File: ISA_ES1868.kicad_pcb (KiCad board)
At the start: 2 copper layers, 104.1 x 102.9 mm, 14 parts, among them J1 ISA BUS

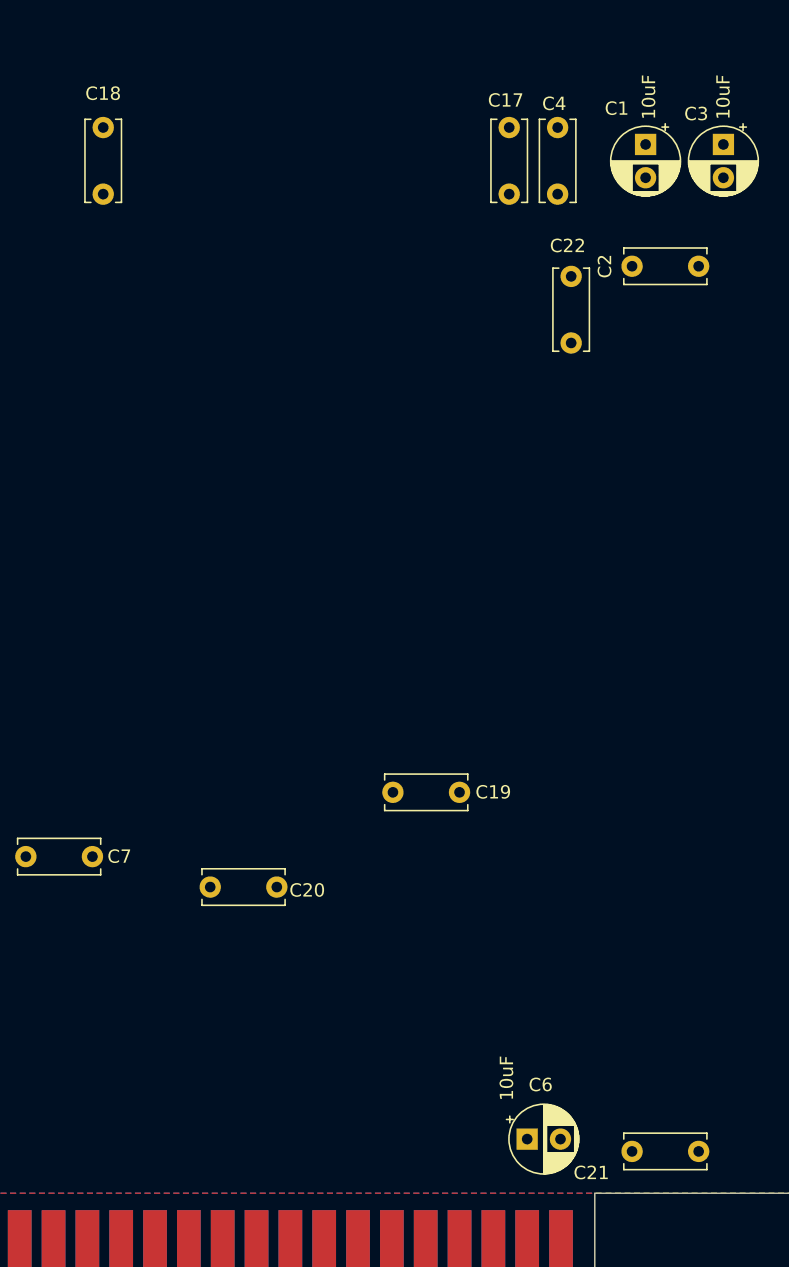
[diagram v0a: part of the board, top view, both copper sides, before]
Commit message: Remove some unused connections from edge
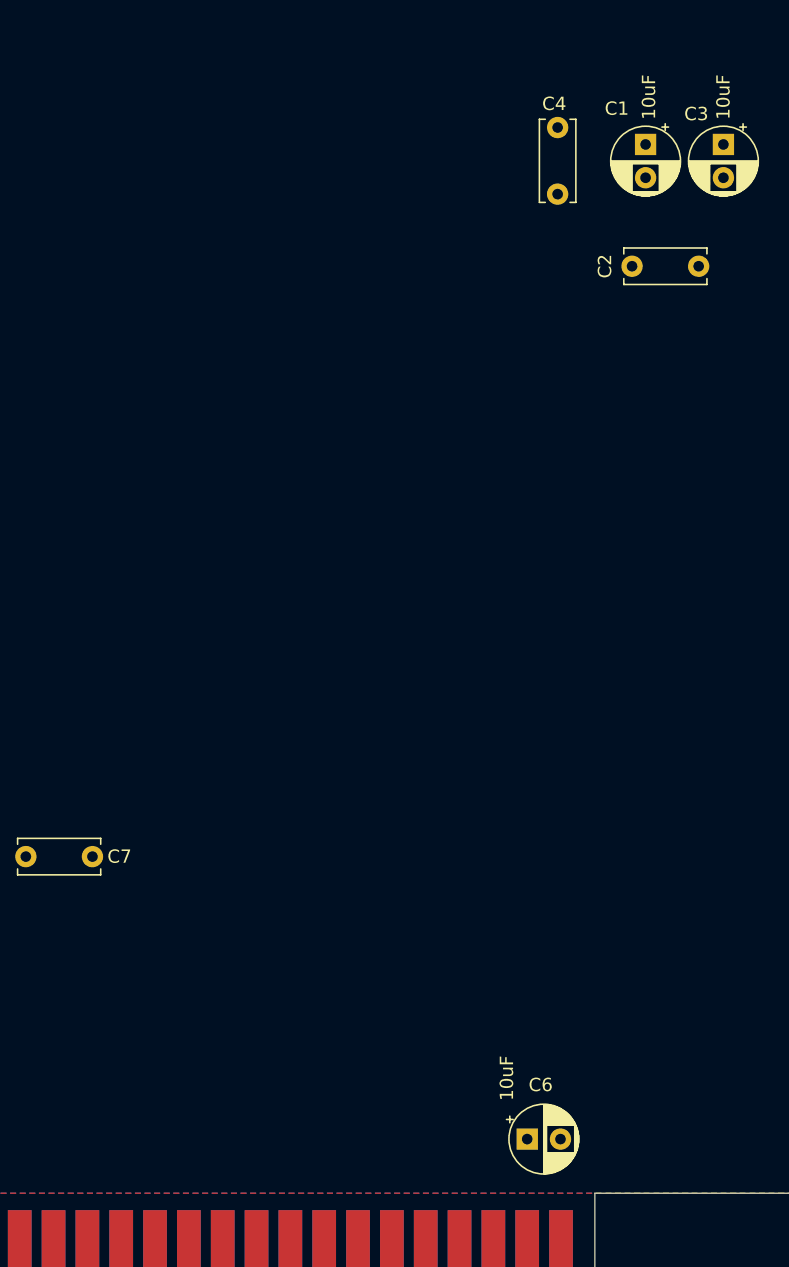
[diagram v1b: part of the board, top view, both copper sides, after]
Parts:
- removed C17, C18, C19, C20, C21, C22: 100nF, Capacitor_THT:C_Disc_D6.0mm_W2.5mm_P5.00mm

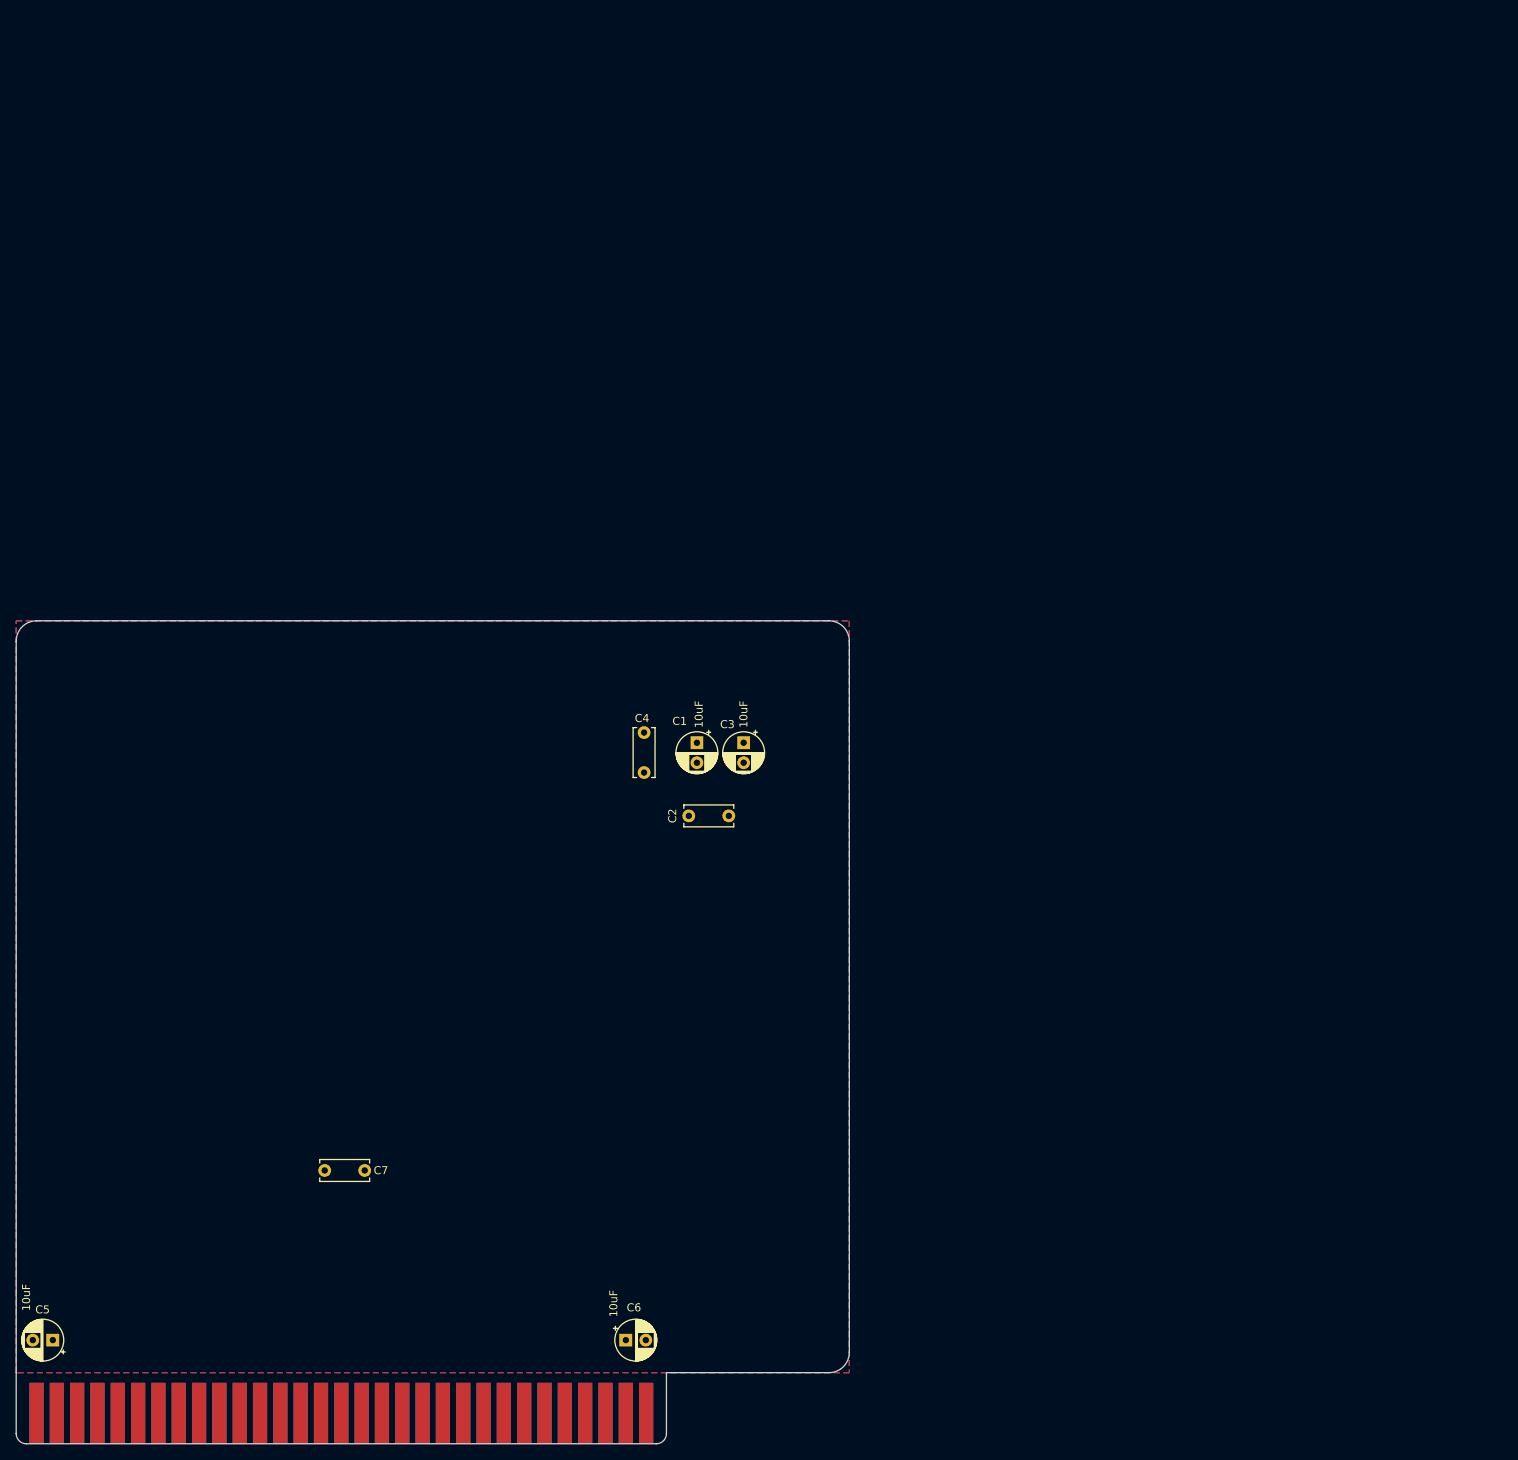
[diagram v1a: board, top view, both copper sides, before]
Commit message: Complete schematics, assigned footprints
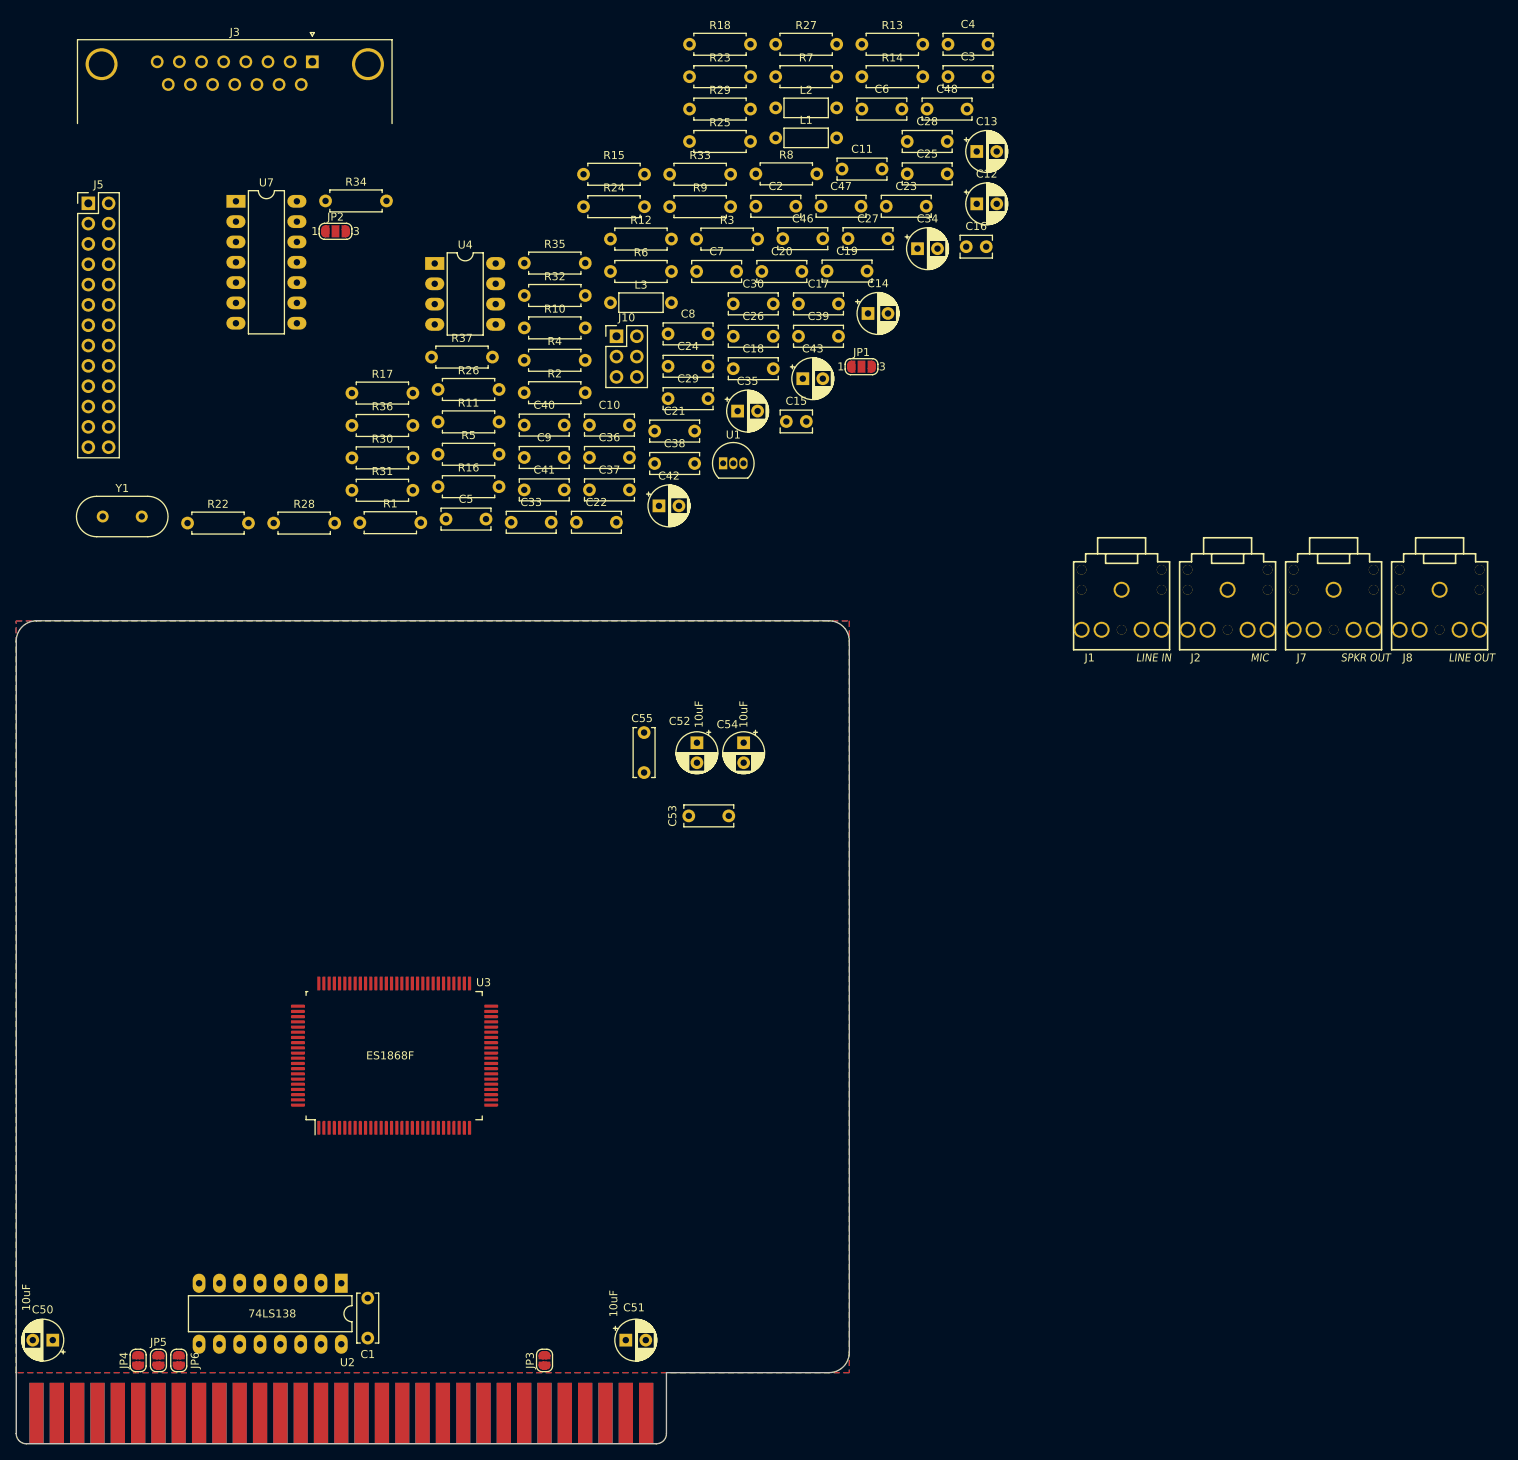
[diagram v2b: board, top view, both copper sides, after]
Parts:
- added C10: 1nF, Capacitor_THT:C_Disc_D6.0mm_W2.5mm_P5.00mm, F.Cu at (282.5, 75.9)
- added C11: 100nF, Capacitor_THT:C_Disc_D6.0mm_W2.5mm_P5.00mm, F.Cu at (314.0, 43.9)
- added C12: 10uF, Capacitor_THT:CP_Radial_D5.0mm_P2.50mm, F.Cu at (330.9, 48.2)
- added C13: 10uF, Capacitor_THT:CP_Radial_D5.0mm_P2.50mm, F.Cu at (330.9, 41.7)
- added C14: 47uF, Capacitor_THT:CP_Radial_D5.0mm_P2.50mm, F.Cu at (317.3, 61.9)
- added C15: 10pF, Capacitor_THT:C_Disc_D3.8mm_W2.6mm_P2.50mm, F.Cu at (307.1, 75.4)
- added C16: 10pF, Capacitor_THT:C_Disc_D3.8mm_W2.6mm_P2.50mm, F.Cu at (329.6, 53.6)
- added C17: 100nF, Capacitor_THT:C_Disc_D6.0mm_W2.5mm_P5.00mm, F.Cu at (308.6, 60.7)
- added C18: 10nF, Capacitor_THT:C_Disc_D6.0mm_W2.5mm_P5.00mm, F.Cu at (300.5, 68.8)
- added C19: 10nF, Capacitor_THT:C_Disc_D6.0mm_W2.5mm_P5.00mm, F.Cu at (312.2, 56.6)
- added C2: 100nF, Capacitor_THT:C_Disc_D6.0mm_W2.5mm_P5.00mm, F.Cu at (303.3, 48.5)
- added C20: 10nF, Capacitor_THT:C_Disc_D6.0mm_W2.5mm_P5.00mm, F.Cu at (304.0, 56.7)
- added C21: 10nF, Capacitor_THT:C_Disc_D6.0mm_W2.5mm_P5.00mm, F.Cu at (290.6, 76.6)
- added C22: 150pF, Capacitor_THT:C_Disc_D6.0mm_W2.5mm_P5.00mm, F.Cu at (280.8, 88.0)
- added C23: 10nF, Capacitor_THT:C_Disc_D6.0mm_W2.5mm_P5.00mm, F.Cu at (319.6, 48.5)
- added C24: 10nF, Capacitor_THT:C_Disc_D6.0mm_W2.5mm_P5.00mm, F.Cu at (292.3, 68.5)
- added C25: 10nF, Capacitor_THT:C_Disc_D6.0mm_W2.5mm_P5.00mm, F.Cu at (322.2, 44.5)
- added C26: 10nF, Capacitor_THT:C_Disc_D6.0mm_W2.5mm_P5.00mm, F.Cu at (300.5, 64.8)
- added C27: 220nF, Capacitor_THT:C_Disc_D6.0mm_W2.5mm_P5.00mm, F.Cu at (314.8, 52.6)
- added C28: 220nF, Capacitor_THT:C_Disc_D6.0mm_W2.5mm_P5.00mm, F.Cu at (322.2, 40.4)
- added C29: 220nF, Capacitor_THT:C_Disc_D6.0mm_W2.5mm_P5.00mm, F.Cu at (292.3, 72.6)
- added C3: 100nF, Capacitor_THT:C_Disc_D6.0mm_W2.5mm_P5.00mm, F.Cu at (327.3, 32.3)
- added C30: 220nF, Capacitor_THT:C_Disc_D6.0mm_W2.5mm_P5.00mm, F.Cu at (300.5, 60.7)
- added C33: 1nF, Capacitor_THT:C_Disc_D6.0mm_W2.5mm_P5.00mm, F.Cu at (272.7, 88.0)
- added C34: 470uF, Capacitor_THT:CP_Radial_D5.0mm_P2.50mm, F.Cu at (323.5, 53.8)
- added C35: 470uF, Capacitor_THT:CP_Radial_D5.0mm_P2.50mm, F.Cu at (301.0, 74.1)
- added C36: 10uF, Capacitor_THT:C_Disc_D6.0mm_W2.5mm_P5.00mm, F.Cu at (282.5, 79.9)
- added C37: 10uF, Capacitor_THT:C_Disc_D6.0mm_W2.5mm_P5.00mm, F.Cu at (282.5, 84.0)
- added C38: 10nF, Capacitor_THT:C_Disc_D6.0mm_W2.5mm_P5.00mm, F.Cu at (290.6, 80.7)
- added C39: 10nF, Capacitor_THT:C_Disc_D6.0mm_W2.5mm_P5.00mm, F.Cu at (308.6, 64.8)
- added C4: 100nF, Capacitor_THT:C_Disc_D6.0mm_W2.5mm_P5.00mm, F.Cu at (327.3, 28.3)
- added C40: 100nF, Capacitor_THT:C_Disc_D6.0mm_W2.5mm_P5.00mm, F.Cu at (274.3, 75.9)
- added C41: 100nF, Capacitor_THT:C_Disc_D6.0mm_W2.5mm_P5.00mm, F.Cu at (274.3, 84.0)
- added C42: 100uF, Capacitor_THT:CP_Radial_D5.0mm_P2.50mm, F.Cu at (291.2, 86.0)
- added C43: 47uF, Capacitor_THT:CP_Radial_D5.0mm_P2.50mm, F.Cu at (309.1, 70.1)
- added C46: 1nF, Capacitor_THT:C_Disc_D6.0mm_W2.5mm_P5.00mm, F.Cu at (306.6, 52.6)
- added C47: 220nF, Capacitor_THT:C_Disc_D6.0mm_W2.5mm_P5.00mm, F.Cu at (311.4, 48.5)
- added C48: 220nF, Capacitor_THT:C_Disc_D6.0mm_W2.5mm_P5.00mm, F.Cu at (324.7, 36.4)
- added C5: 100nF, Capacitor_THT:C_Disc_D6.0mm_W2.5mm_P5.00mm, F.Cu at (264.5, 87.6)
- added C6: 100nF, Capacitor_THT:C_Disc_D6.0mm_W2.5mm_P5.00mm, F.Cu at (316.5, 36.4)
- added C7: 100nF, Capacitor_THT:C_Disc_D6.0mm_W2.5mm_P5.00mm, F.Cu at (295.9, 56.7)
- added C8: 220nF, Capacitor_THT:C_Disc_D6.0mm_W2.5mm_P5.00mm, F.Cu at (292.3, 64.5)
- added C9: 220nF, Capacitor_THT:C_Disc_D6.0mm_W2.5mm_P5.00mm, F.Cu at (274.3, 79.9)
- added J1: LINE IN, My_Components:Conn_Audio_3.5mm_Stereo_SJ1-352XNG, F.Cu at (349.0, 91.9)
- added J10: Volume buttons, Connector_PinHeader_2.54mm:PinHeader_2x03_P2.54mm_Vertical, F.Cu at (285.9, 64.8)
- added J2: MIC, My_Components:Conn_Audio_3.5mm_Stereo_SJ1-352XNG, F.Cu at (362.2, 91.9)
- added J3: Joystick/MIDI, Connector_Dsub:DSUB-15_Female_Horizontal_P2.77x2.84mm_EdgePinOffset4.94mm_Housed_MountingHolesOffset7.48mm, F.Cu at (247.8, 30.5)
- added J5: Wavetable, Connector_PinHeader_2.54mm:PinHeader_2x13_P2.54mm_Vertical, F.Cu at (219.8, 48.1)
- added J7: SPKR OUT, My_Components:Conn_Audio_3.5mm_Stereo_SJ1-352XNG, F.Cu at (375.5, 91.9)
- added J8: LINE OUT, My_Components:Conn_Audio_3.5mm_Stereo_SJ1-352XNG, F.Cu at (388.7, 91.9)
- added JP1: Intl. ROM 1, Jumper:SolderJumper-3_P1.3mm_Open_RoundedPad1.0x1.5mm_NumberLabels, F.Cu at (316.5, 68.6)
- added JP2: Intl. ROM 2, Jumper:SolderJumper-3_P1.3mm_Open_RoundedPad1.0x1.5mm_NumberLabels, F.Cu at (250.7, 51.6)
- added JP3: ~DRQ2~ Jumper, Jumper:SolderJumper-2_P1.3mm_Open_RoundedPad1.0x1.5mm, F.Cu at (276.9, 192.8)
- added JP4: ~DACK2~ Jumper, Jumper:SolderJumper-2_P1.3mm_Open_RoundedPad1.0x1.5mm, F.Cu at (226.1, 192.8)
- added JP5: IRQ3 Jumper, Jumper:SolderJumper-2_P1.3mm_Open_RoundedPad1.0x1.5mm, F.Cu at (228.6, 192.8)
- added JP6: IRQ4 Jumper, Jumper:SolderJumper-2_P1.3mm_Open_RoundedPad1.0x1.5mm, F.Cu at (231.1, 192.8)
- added L1: Ferrite Bead, Inductor_THT:L_Axial_L5.3mm_D2.2mm_P7.62mm_Horizontal_Vishay_IM-1, F.Cu at (305.8, 40.0)
- added L2: Ferrite Bead, Inductor_THT:L_Axial_L5.3mm_D2.2mm_P7.62mm_Horizontal_Vishay_IM-1, F.Cu at (305.8, 36.2)
- added L3: Ferrite Bead, Inductor_THT:L_Axial_L5.3mm_D2.2mm_P7.62mm_Horizontal_Vishay_IM-1, F.Cu at (285.1, 60.6)
- added R1: 7.5k, Resistor_THT:R_Axial_DIN0207_L6.3mm_D2.5mm_P7.62mm_Horizontal, F.Cu at (253.8, 88.1)
- added R10: 2.2k, Resistor_THT:R_Axial_DIN0207_L6.3mm_D2.5mm_P7.62mm_Horizontal, F.Cu at (274.3, 63.7)
- added R11: 2.2k, Resistor_THT:R_Axial_DIN0207_L6.3mm_D2.5mm_P7.62mm_Horizontal, F.Cu at (263.6, 75.5)
- added R12: 2.2k, Resistor_THT:R_Axial_DIN0207_L6.3mm_D2.5mm_P7.62mm_Horizontal, F.Cu at (285.1, 52.6)
- added R13: 2.2k, Resistor_THT:R_Axial_DIN0207_L6.3mm_D2.5mm_P7.62mm_Horizontal, F.Cu at (316.5, 28.3)
- added R14: 1k, Resistor_THT:R_Axial_DIN0207_L6.3mm_D2.5mm_P7.62mm_Horizontal, F.Cu at (316.5, 32.3)
- added R15: 1k, Resistor_THT:R_Axial_DIN0207_L6.3mm_D2.5mm_P7.62mm_Horizontal, F.Cu at (281.7, 44.5)
- added R16: 1k, Resistor_THT:R_Axial_DIN0207_L6.3mm_D2.5mm_P7.62mm_Horizontal, F.Cu at (263.6, 83.6)
- added R17: 1k, Resistor_THT:R_Axial_DIN0207_L6.3mm_D2.5mm_P7.62mm_Horizontal, F.Cu at (252.8, 71.9)
- added R18: 22k, Resistor_THT:R_Axial_DIN0207_L6.3mm_D2.5mm_P7.62mm_Horizontal, F.Cu at (295.0, 28.3)
- added R2: 7.5k, Resistor_THT:R_Axial_DIN0207_L6.3mm_D2.5mm_P7.62mm_Horizontal, F.Cu at (274.3, 71.8)
- added R22: 33k, Resistor_THT:R_Axial_DIN0207_L6.3mm_D2.5mm_P7.62mm_Horizontal, F.Cu at (232.2, 88.1)
- added R23: 33k, Resistor_THT:R_Axial_DIN0207_L6.3mm_D2.5mm_P7.62mm_Horizontal, F.Cu at (295.0, 32.3)
- added R24: 820k, Resistor_THT:R_Axial_DIN0207_L6.3mm_D2.5mm_P7.62mm_Horizontal, F.Cu at (281.7, 48.6)
- added R25: 820k, Resistor_THT:R_Axial_DIN0207_L6.3mm_D2.5mm_P7.62mm_Horizontal, F.Cu at (295.0, 40.4)
- added R26: 820k, Resistor_THT:R_Axial_DIN0207_L6.3mm_D2.5mm_P7.62mm_Horizontal, F.Cu at (263.6, 71.4)
- added R27: 820k, Resistor_THT:R_Axial_DIN0207_L6.3mm_D2.5mm_P7.62mm_Horizontal, F.Cu at (305.8, 28.3)
- added R28: 2.7, Resistor_THT:R_Axial_DIN0207_L6.3mm_D2.5mm_P7.62mm_Horizontal, F.Cu at (243.0, 88.1)
- added R29: 2.7, Resistor_THT:R_Axial_DIN0207_L6.3mm_D2.5mm_P7.62mm_Horizontal, F.Cu at (295.0, 36.4)
- added R3: 2.2k, Resistor_THT:R_Axial_DIN0207_L6.3mm_D2.5mm_P7.62mm_Horizontal, F.Cu at (295.9, 52.6)
- added R30: 15k, Resistor_THT:R_Axial_DIN0207_L6.3mm_D2.5mm_P7.62mm_Horizontal, F.Cu at (252.8, 80.0)
- added R31: 15k, Resistor_THT:R_Axial_DIN0207_L6.3mm_D2.5mm_P7.62mm_Horizontal, F.Cu at (252.8, 84.0)
- added R32: 10k, Resistor_THT:R_Axial_DIN0207_L6.3mm_D2.5mm_P7.62mm_Horizontal, F.Cu at (274.3, 59.7)
- added R33: 10k, Resistor_THT:R_Axial_DIN0207_L6.3mm_D2.5mm_P7.62mm_Horizontal, F.Cu at (292.5, 44.5)
- added R34: 1M, Resistor_THT:R_Axial_DIN0207_L6.3mm_D2.5mm_P7.62mm_Horizontal, F.Cu at (249.5, 47.8)
- added R35: 1M, Resistor_THT:R_Axial_DIN0207_L6.3mm_D2.5mm_P7.62mm_Horizontal, F.Cu at (274.3, 55.6)
- added R36: 1M, Resistor_THT:R_Axial_DIN0207_L6.3mm_D2.5mm_P7.62mm_Horizontal, F.Cu at (252.8, 75.9)
- added R37: 1M, Resistor_THT:R_Axial_DIN0207_L6.3mm_D2.5mm_P7.62mm_Horizontal, F.Cu at (262.7, 67.4)
- added R4: 2.2k, Resistor_THT:R_Axial_DIN0207_L6.3mm_D2.5mm_P7.62mm_Horizontal, F.Cu at (274.3, 67.8)
- added R5: 2.2k, Resistor_THT:R_Axial_DIN0207_L6.3mm_D2.5mm_P7.62mm_Horizontal, F.Cu at (263.6, 79.5)
- added R6: 2.2k, Resistor_THT:R_Axial_DIN0207_L6.3mm_D2.5mm_P7.62mm_Horizontal, F.Cu at (285.1, 56.7)
- added R7: 10k, Resistor_THT:R_Axial_DIN0207_L6.3mm_D2.5mm_P7.62mm_Horizontal, F.Cu at (305.8, 32.3)
- added R8: 2.2k, Resistor_THT:R_Axial_DIN0207_L6.3mm_D2.5mm_P7.62mm_Horizontal, F.Cu at (303.3, 44.5)
- added R9: 2.2k, Resistor_THT:R_Axial_DIN0207_L6.3mm_D2.5mm_P7.62mm_Horizontal, F.Cu at (292.5, 48.6)
- added U1: L78L05_TO92, Package_TO_SOT_THT:TO-92_Inline, F.Cu at (299.2, 80.6)
- added U2: 74LS138, Package_DIP:DIP-16_W7.62mm_LongPads, F.Cu at (251.5, 183.1)
- added U3: ES1868F, Package_QFP:LQFP-14x20mm_P0.5mm, F.Cu at (258.1, 154.7)
- added U4: 93LC66, Package_DIP:DIP-8_W7.62mm_LongPads, F.Cu at (263.1, 55.7)
- added U7: LM1877, Package_DIP:DIP-14_W7.62mm_LongPads, F.Cu at (238.3, 47.9)
- added Y1: 14.318Mhz, Crystal:Crystal_HC49-4H_Vertical, F.Cu at (221.6, 87.3)
- moved C1 21.0 mm to (254.8, 190.0), turned to 90 degrees
- renumbered C7 to C1, C5 to C50, C6 to C51, C1 to C52, C2 to C53, C3 to C54, C4 to C55, J1 to J11
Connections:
- J11 pad 13: (no net) -> /~IOW
- J11 pad 14: (no net) -> /~IOR
- J11 pad 15: (no net) -> /~DACK3
- J11 pad 16: (no net) -> /DRQ3
- J11 pad 17: (no net) -> /~DACK1
- J11 pad 18: (no net) -> /DRQ1
- J11 pad 2: (no net) -> /RESETDRV
- J11 pad 21: (no net) -> /IRQ7
- J11 pad 23: (no net) -> /IRQ5
- J11 pad 24: (no net) -> /IRQ4
- J11 pad 25: (no net) -> /IRQ3
- J11 pad 26: (no net) -> /~DACK2
- J11 pad 33: (no net) -> /D7
- J11 pad 34: (no net) -> /D6
- J11 pad 35: (no net) -> /D5
- J11 pad 36: (no net) -> /D4
- J11 pad 37: (no net) -> /D3
- J11 pad 38: (no net) -> /D2
- J11 pad 39: (no net) -> /D1
- J11 pad 4: (no net) -> /IRQ9
- J11 pad 40: (no net) -> /D0
- J11 pad 42: (no net) -> /AEN
- J11 pad 47: (no net) -> /A15
- J11 pad 48: (no net) -> /A14
- J11 pad 49: (no net) -> /A13
- J11 pad 50: (no net) -> /A12
- J11 pad 51: (no net) -> /A11
- J11 pad 52: (no net) -> /A10
- J11 pad 53: (no net) -> /A9
- J11 pad 54: (no net) -> /A8
- J11 pad 55: (no net) -> /A7
- J11 pad 56: (no net) -> /A6
- J11 pad 57: (no net) -> /A5
- J11 pad 58: (no net) -> /A4
- J11 pad 59: (no net) -> /A3
- J11 pad 6: (no net) -> /DRQ2
- J11 pad 60: (no net) -> /A2
- J11 pad 61: (no net) -> /A1
- J11 pad 62: (no net) -> /A0
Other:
- copper layers 2 -> 4

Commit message: Change some output options
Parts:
- J8: footprint My_Components:Conn_Audio_3.5mm_Stereo_SJ1-352XNG -> Connector_PinSocket_2.54mm:PinSocket_1x03_P2.54mm_Vertical
- moved J3 145.5 mm to (307.6, 163.1), turned to 90 degrees
- moved J8 71.9 mm to (317.5, 101.3)
- moved J7 42.0 mm to (363.5, 132.2), turned to 270 degrees
- moved J2 27.0 mm to (363.5, 118.9), turned to 270 degrees
- moved J1 19.9 mm to (363.5, 105.7), turned to 270 degrees
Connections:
- J8 pad 1: GNDA -> Net-(C36-Pad2)
- J8 pad 3: Net-(C36-Pad2) -> GNDA
